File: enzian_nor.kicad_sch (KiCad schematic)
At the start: 27 parts, among them IC1 L7809ABD2T-TR, J1 ASP-134488-01, U1 MT35XU02GCBA1G12-0AUT

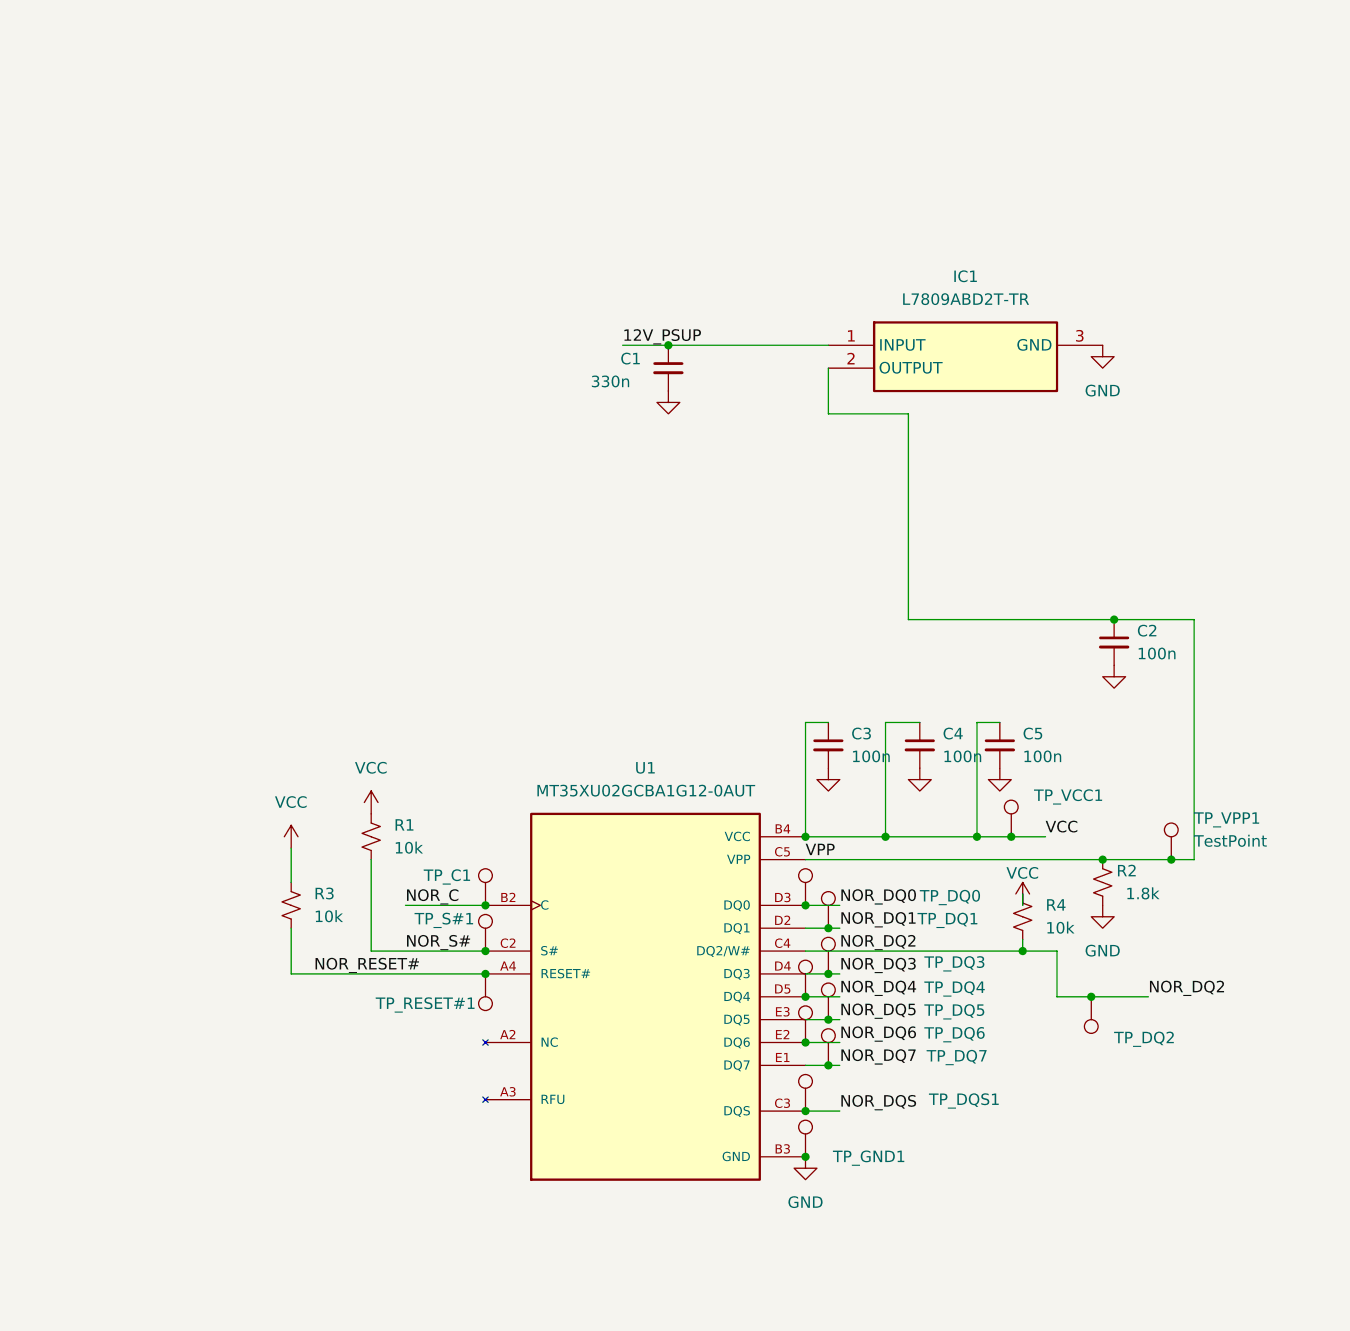
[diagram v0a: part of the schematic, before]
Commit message: Add version number, mounting holes, and minor changes to via placement
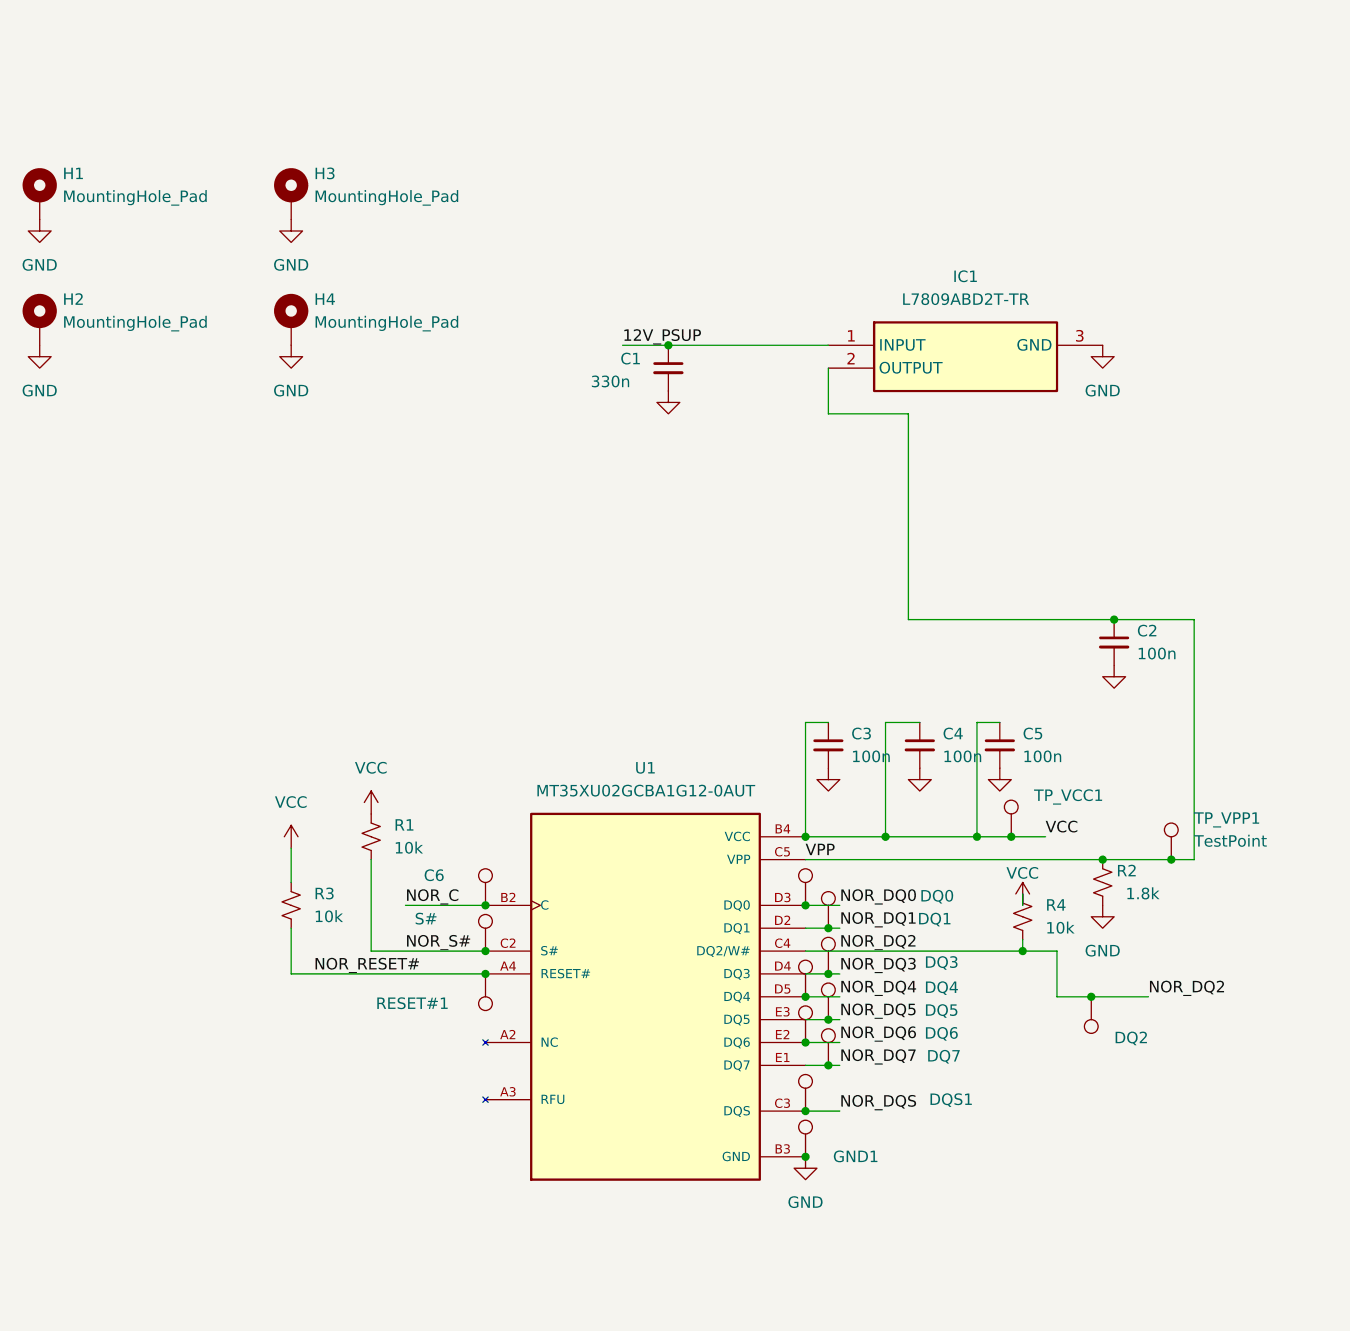
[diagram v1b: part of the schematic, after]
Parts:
- added H1, H2, H3, H4: MountingHole_Pad, MountingHole:MountingHole_3.2mm_M3_Pad_Via, symbol Mechanical:MountingHole_Pad
- renumbered TP_C1 to C6, TP_DQ0 to DQ0, TP_DQ1 to DQ1, TP_DQ2 to DQ2, TP_DQ3 to DQ3, TP_DQ4 to DQ4, TP_DQ5 to DQ5, TP_DQ6 to DQ6, TP_DQ7 to DQ7, TP_DQS1 to DQS1, TP_GND1 to GND1, TP_RESET#1 to RESET#1, TP_S#1 to S#
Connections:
- net GND: now also H1.1, H2.1, H3.1, H4.1
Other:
- company: (none) -> Stanford SING group (David Shim)
- title: (none) -> NOR LtRAM Daughterboard

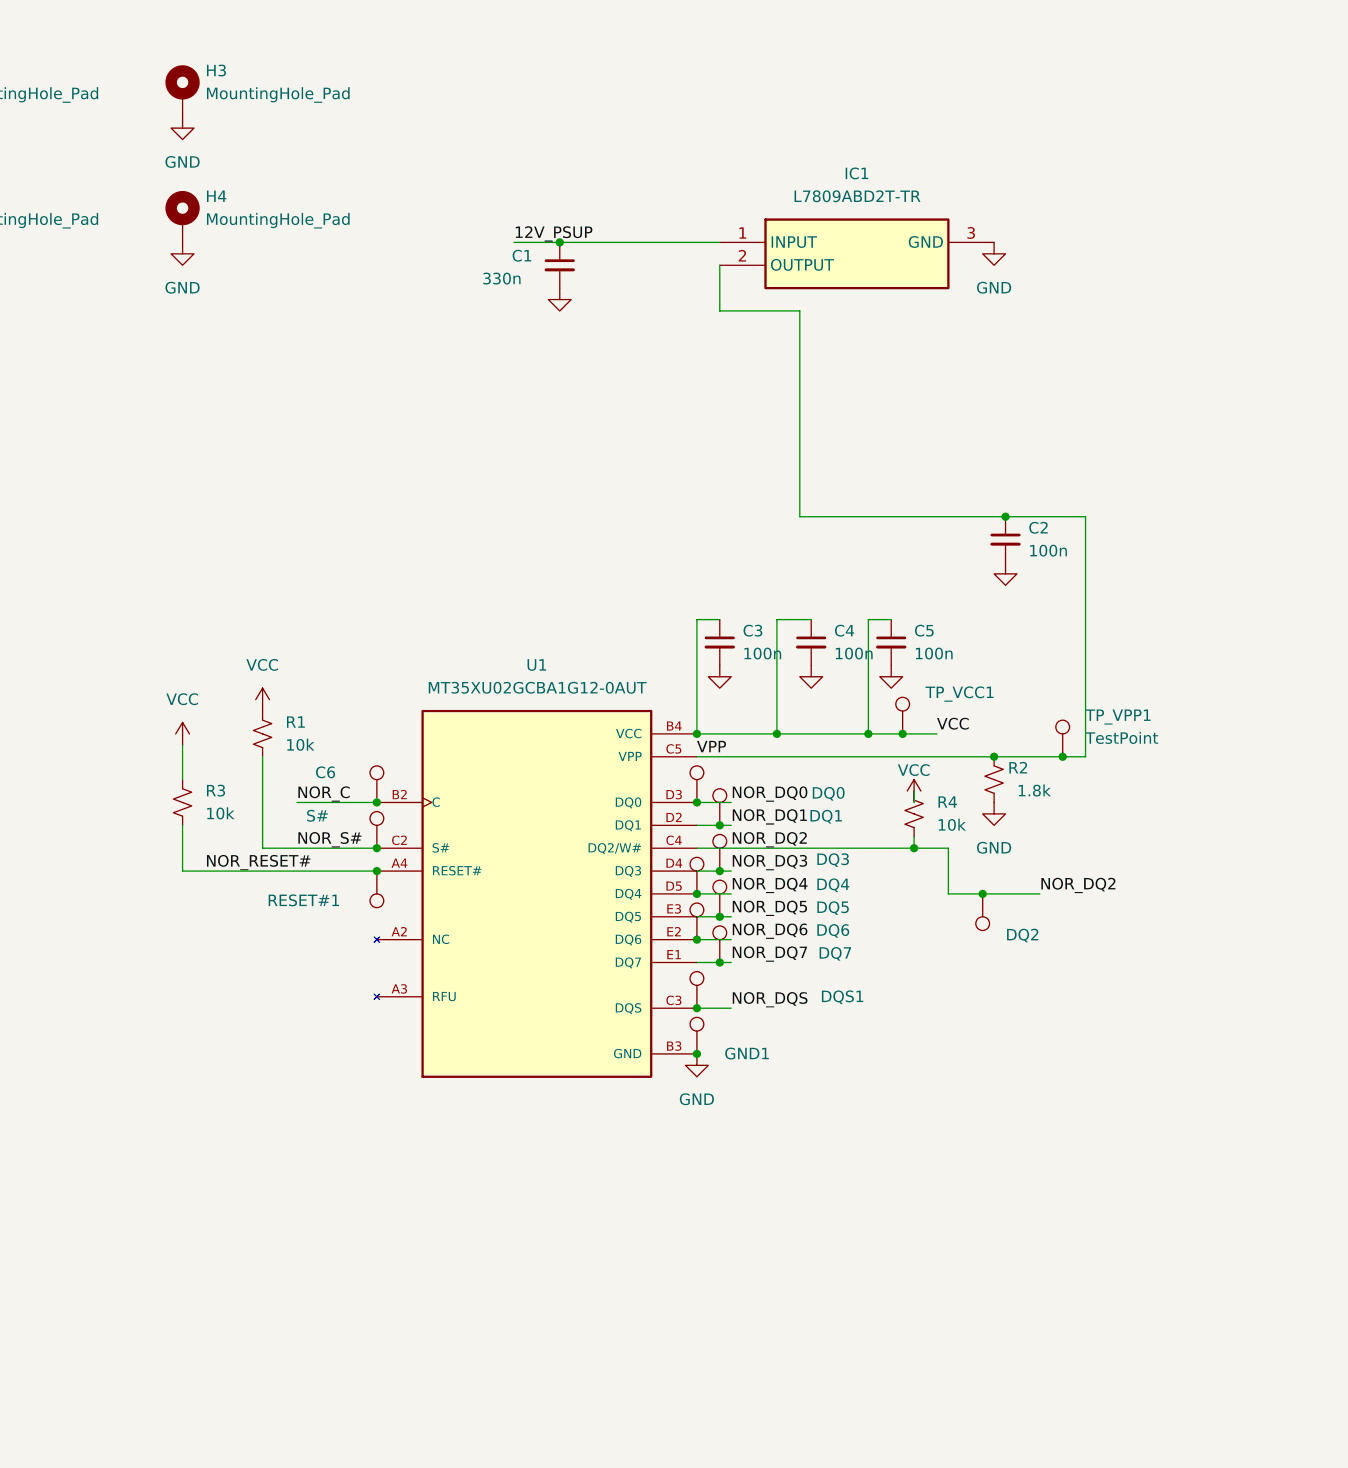
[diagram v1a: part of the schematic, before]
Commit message: Update schematics along with the pcb design
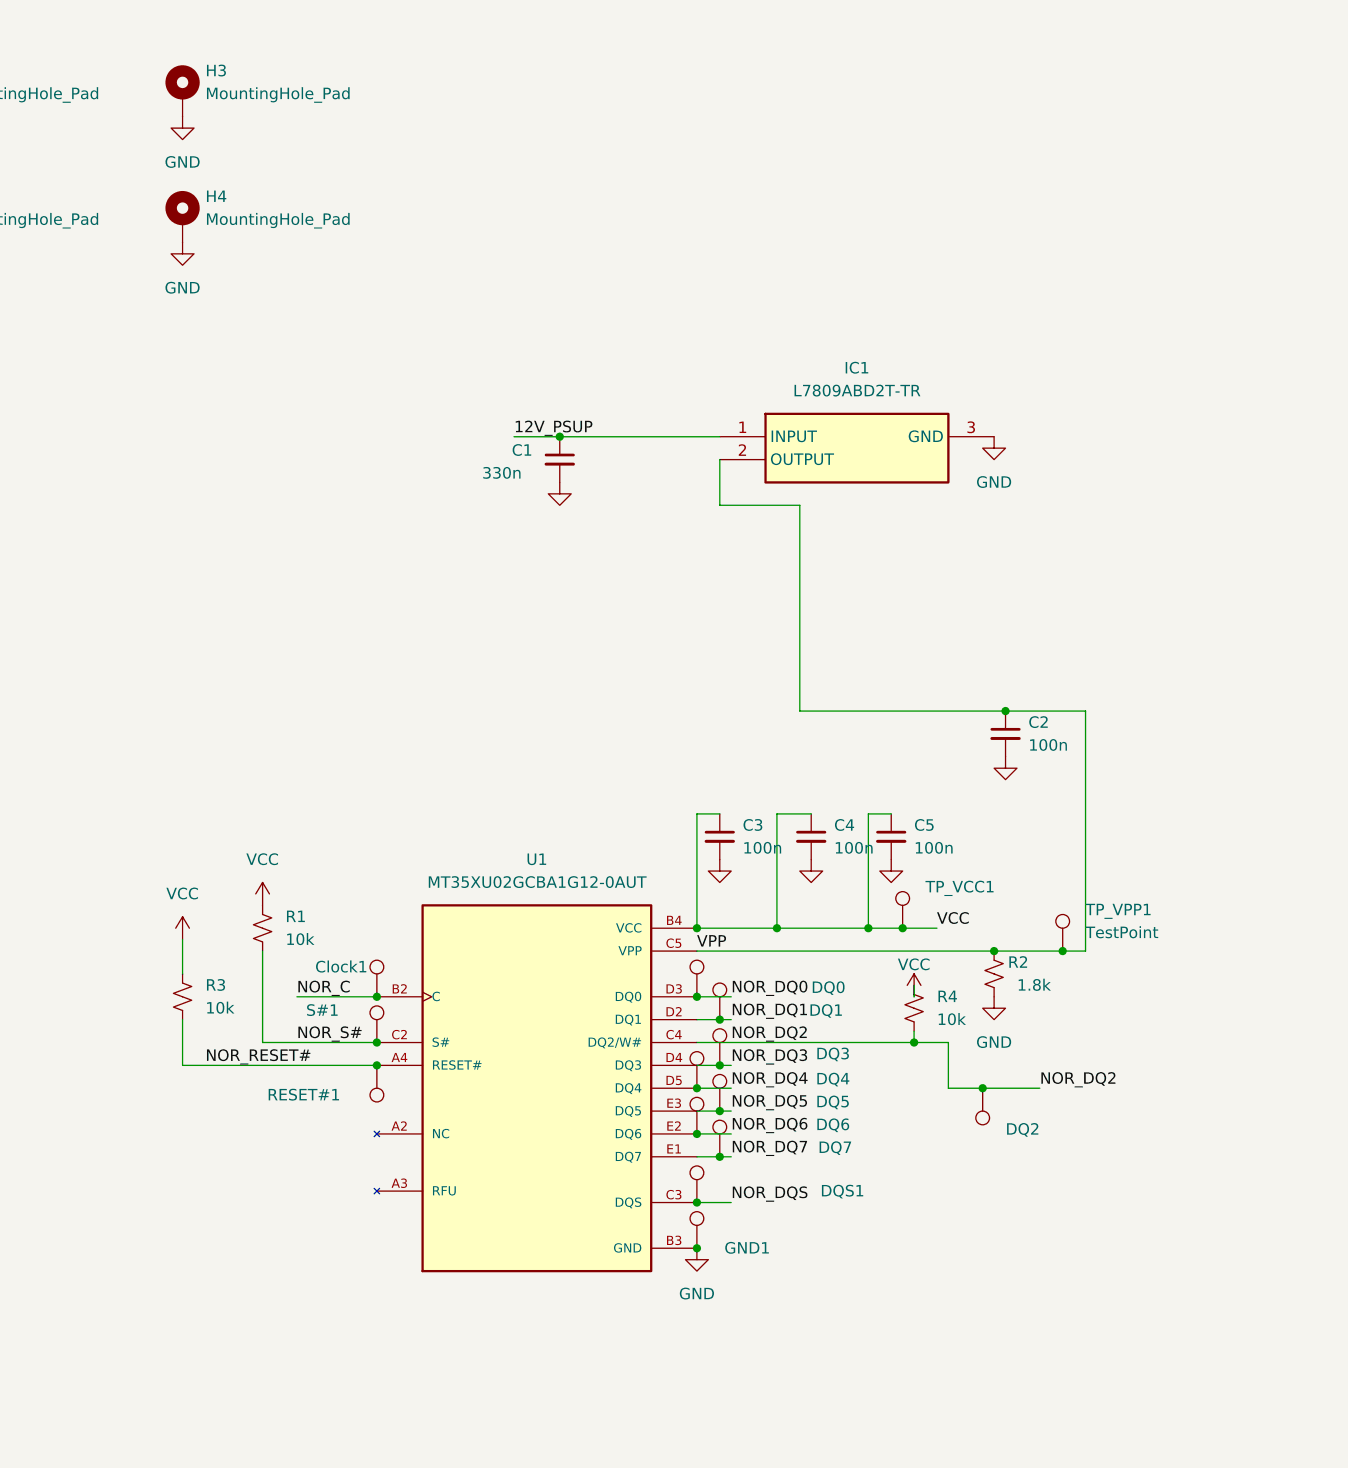
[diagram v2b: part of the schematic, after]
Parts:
- renumbered C6 to Clock1, S# to S#1
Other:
- moved on the sheet: C1, C2, C3, C4, C5, Clock1, DQ0, DQ1, DQ2, DQ3, DQ4, DQ5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

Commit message: Applied Mark's suggestions
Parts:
- removed C3, C5: 100n, Capacitor_SMD:C_0805_2012Metric, symbol Device:C_Small
- added C4: 100n, Capacitor_SMD:C_0805_2012Metric, symbol Device:C_Small
- renumbered C4 to C3
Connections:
- net GND: now also J1.A1, J1.A12, J1.A13, J1.A16, J1.A17, J1.A20, J1.A21, J1.A24, J1.A25, J1.A28, J1.A29, J1.A32, J1.A33, J1.A36, J1.A37, J1.A4, J1.A40, J1.A5, J1.A8, J1.A9, J1.B10, J1.B11, J1.B14, J1.B15, J1.B18, J1.B19, J1.B2, J1.B22, J1.B23, J1.B26, J1.B27, J1.B3, J1.B30, J1.B31, J1.B34, J1.B35, J1.B38, J1.B39, J1.B6, J1.B7, J1.C1, J1.C12, J1.C13, J1.C16, J1.C17, J1.C20, J1.C21, J1.C24, J1.C25, J1.C28, J1.C29, J1.C32, J1.C33, J1.C34, J1.C36, J1.C38, J1.C4, J1.C40, J1.C5, J1.C8, J1.C9, J1.D10, J1.D13, J1.D16, J1.D19, J1.D2, J1.D22, J1.D25, J1.D28, J1.D3, J1.D35, J1.D37, J1.D39, J1.D6, J1.D7, J1.E1, J1.E11, J1.E14, J1.E17, J1.E20, J1.E23, J1.E26, J1.E29, J1.E32, J1.E35, J1.E38, J1.E4, J1.E40, J1.E5, J1.E8, J1.F12, J1.F15, J1.F18, J1.F2, J1.F21, J1.F24, J1.F27, J1.F3, J1.F30, J1.F33, J1.F36, J1.F39, J1.F6, J1.F9, J1.G1, J1.G11, J1.G14, J1.G17, J1.G20, J1.G23, J1.G26, J1.G29, J1.G32, J1.G35, J1.G38, J1.G4, J1.G40, J1.G5, J1.G8, J1.H12, J1.H15, J1.H18, J1.H21, J1.H24, J1.H27, J1.H3, J1.H30, J1.H33, J1.H36, J1.H39, J1.H6, J1.H9, J1.J1, J1.J11, J1.J14, J1.J17, J1.J20, J1.J23, J1.J26, J1.J29, J1.J32, J1.J35, J1.J38, J1.J4, J1.J40, J1.J5, J1.J8, J1.K12, J1.K15, J1.K18, J1.K2, J1.K21, J1.K24, J1.K27, J1.K3, J1.K30, J1.K33, J1.K36, J1.K39, J1.K6, J1.K9, C4.2
- net VCC: now also C4.1
- no-connect marks 386 -> 225
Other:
- moved on the sheet: C3

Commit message: Added all 1V8 power pins to schematic and PCB
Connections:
- net VCC: now also J1.E39, J1.F40, J1.H40
- no-connect marks 225 -> 222
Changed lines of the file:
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@@
 	)
 	(no_connect
-		(at 209.55 440.69)
-	)
-	(no_connect
 		(at 234.95 54.61)
 	)
@@
 	)
 	(no_connect
-		(at 234.95 36.83)
-	)
-	(no_connect
 		(at 209.55 11.43)
 	)
@@
 	)
 	(no_connect
-		(at 234.95 240.03)
-	)
-	(no_connect
 		(at 209.55 367.03)
 	)
@@
 	(wire
 		(pts
+			(xy 234.95 36.83) (xy 260.35 36.83)
+		)
+		(stroke
+			(width 0)
+			(type default)
+		)
+	)
+	(wire
+		(pts
 			(xy 208.28 135.89) (xy 209.55 135.89)
 		)
@@
 	(wire
 		(pts
+			(xy 209.55 440.69) (xy 184.15 440.69)
+		)
+		(stroke
+			(width 0)
+			(type default)
+		)
+	)
+	(wire
+		(pts
 			(xy 234.95 207.01) (xy 236.22 207.01)
 		)
@@
 	(wire
 		(pts
+			(xy 234.95 240.03) (xy 260.35 240.03)
+		)
+		(stroke
+			(width 0)
+			(type default)
+		)
+	)
+	(wire
+		(pts
 			(xy 234.95 283.21) (xy 236.22 283.21)
 		)
@@
 		)
 	)
+	(label "VCC"
+		(at 184.15 440.69 180)
+		(effects
+			(font
+				(size 1.27 1.27)
+			)
+			(justify right bottom)
+		)
+	)
 	(label "NOR_DQ2"
 		(at 107.95 124.46 0)
@@
 		)
 	)
+	(label "VCC"
+		(at 260.35 36.83 0)
+		(effects
+			(font
+				(size 1.27 1.27)
+			)
+			(justify left bottom)
+		)
+	)
 	(label "12V_PSUP"
 		(at 139.7 185.42 0)
@@
 		(effects
 			(font
+				(size 1.27 1.27)
+			)
+			(justify left bottom)
+		)
+	)
+	(label "VCC"
+		(at 260.35 240.03 0)
+		(effects
+			(font
